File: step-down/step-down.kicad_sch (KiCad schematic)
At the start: 16 parts, among them J1 Conn_01x01_Pin, J2 Conn_01x01_Pin, J4 Conn_01x01_Pin

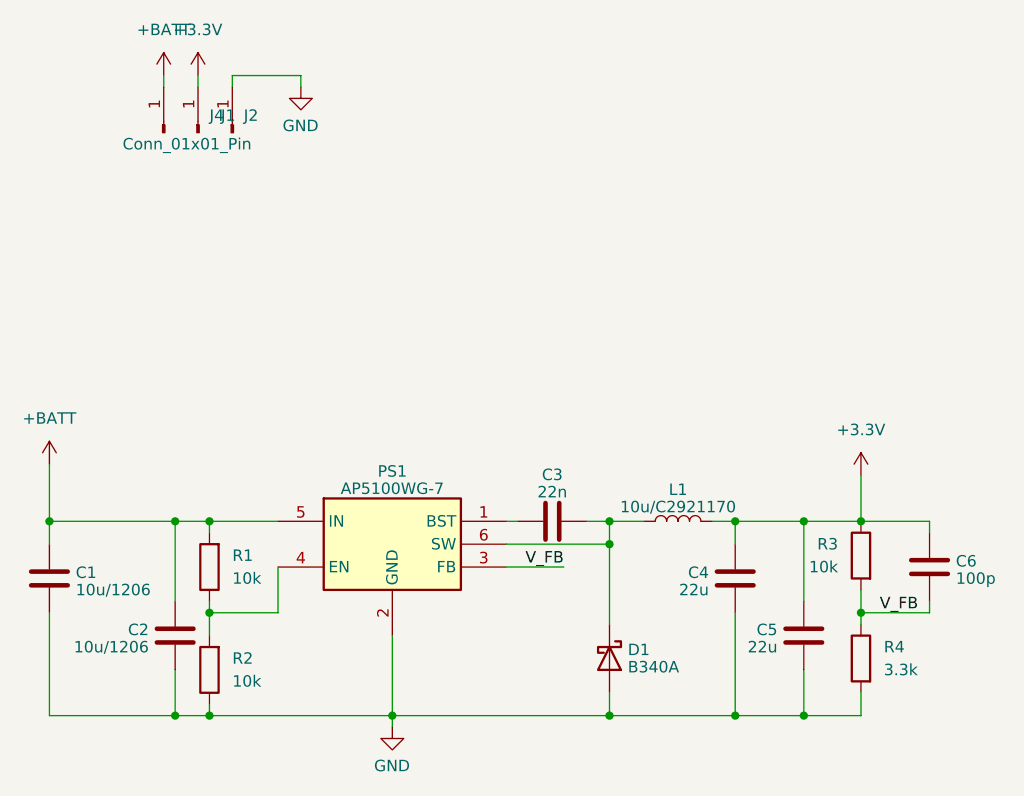
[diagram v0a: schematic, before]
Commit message: moved EN logic to external control
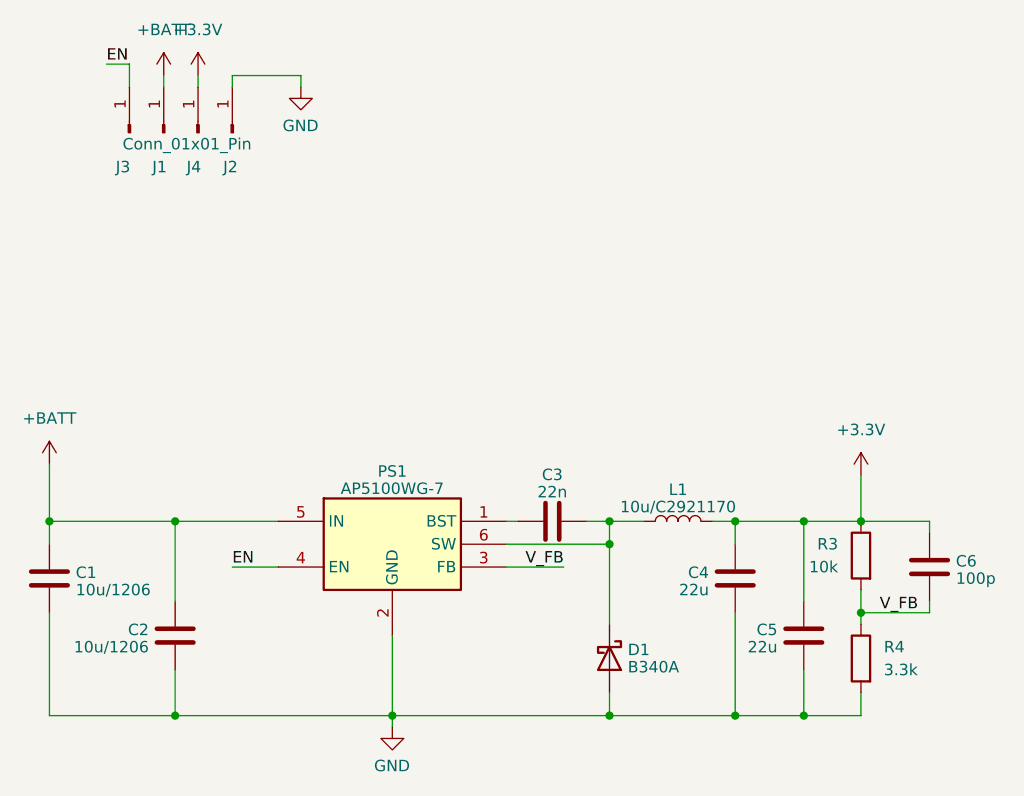
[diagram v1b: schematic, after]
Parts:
- removed R1, R2: 10k, Resistor_SMD:R_0603_1608Metric, symbol Device:R
- added J3: Conn_01x01_Pin, Connector_PinSocket_2.54mm:PinSocket_1x01_P2.54mm_Vertical, symbol Connector:Conn_01x01_Pin
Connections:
- net EN: now reaches PS1.4 (EN)
- net EN: now also J3.1 (Pin_1)
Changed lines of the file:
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@@
 	(paper "A4")
-	(junction
-		(at 109.22 85.09)
-		(diameter 0)
-		(color 0 0 0 0)
-	)
 	(junction
 		(at 91.44 85.09)
@@
 	)
 	(junction
-		(at 109.22 106.68)
-		(diameter 0)
-		(color 0 0 0 0)
-	)
-	(junction
 		(at 105.41 85.09)
 		(diameter 0)
@@
 	)
 	(junction
-		(at 109.22 95.25)
-		(diameter 0)
-		(color 0 0 0 0)
-	)
-	(junction
 		(at 153.67 87.63)
 		(diameter 0)
@@
 	(wire
 		(pts
-			(xy 109.22 97.79) (xy 109.22 95.25)
-		)
-		(stroke
-			(width 0)
-			(type default)
-		)
-	)
-	(wire
-		(pts
 			(xy 189.23 93.98) (xy 189.23 95.25)
 		)
@@
 	(wire
 		(pts
-			(xy 109.22 105.41) (xy 109.22 106.68)
-		)
-		(stroke
-			(width 0)
-			(type default)
-		)
-	)
-	(wire
-		(pts
 			(xy 91.44 78.74) (xy 91.44 85.09)
 		)
@@
 	(wire
 		(pts
-			(xy 109.22 85.09) (xy 109.22 86.36)
-		)
-		(stroke
-			(width 0)
-			(type default)
-		)
-	)
-	(wire
-		(pts
 			(xy 165.1 85.09) (xy 167.64 85.09)
 		)
@@
 	(wire
 		(pts
+			(xy 111.76 90.17) (xy 116.84 90.17)
+		)
+		(stroke
+			(width 0)
+			(type default)
+		)
+	)
+	(wire
+		(pts
 			(xy 91.44 95.25) (xy 91.44 106.68)
 		)
@@
 	(wire
 		(pts
-			(xy 116.84 90.17) (xy 116.84 95.25)
-		)
-		(stroke
-			(width 0)
-			(type default)
-		)
-	)
-	(wire
-		(pts
-			(xy 105.41 106.68) (xy 109.22 106.68)
-		)
-		(stroke
-			(width 0)
-			(type default)
-		)
-	)
-	(wire
-		(pts
 			(xy 181.61 85.09) (xy 189.23 85.09)
 		)
@@
 	(wire
 		(pts
-			(xy 109.22 93.98) (xy 109.22 95.25)
-		)
-		(stroke
-			(width 0)
-			(type default)
-		)
-	)
-	(wire
-		(pts
-			(xy 109.22 106.68) (xy 129.54 106.68)
-		)
-		(stroke
-			(width 0)
-			(type default)
-		)
-	)
-	(wire
-		(pts
-			(xy 109.22 85.09) (xy 116.84 85.09)
+			(xy 105.41 106.68) (xy 129.54 106.68)
+		)
+		(stroke
+			(width 0)
+			(type default)
+		)
+	)
+	(wire
+		(pts
+			(xy 100.33 34.29) (xy 100.33 36.83)
+		)
+		(stroke
+			(width 0)
+			(type default)
+		)
+	)
+	(wire
+		(pts
+			(xy 105.41 85.09) (xy 116.84 85.09)
 		)
 		(stroke
@@
 	(wire
 		(pts
-			(xy 109.22 95.25) (xy 116.84 95.25)
-		)
-		(stroke
-			(width 0)
-			(type default)
-		)
-	)
-	(wire
-		(pts
-			(xy 105.41 85.09) (xy 109.22 85.09)
+			(xy 97.79 34.29) (xy 100.33 34.29)
 		)
 		(stroke
@@
 			)
 			(justify right bottom)
+		)
+	)
+	(label "EN"
+		(at 111.76 90.17 0)
+		(fields_autoplaced yes)
+		(effects
+			(font
+				(size 1.27 1.27)
+			)
+			(justify left bottom)
+		)
+	)
+	(label "EN"
+		(at 97.79 34.29 0)
+		(fields_autoplaced yes)
+		(effects
+			(font
+				(size 1.27 1.27)
+			)
+			(justify left bottom)
 		)
 	)
@@
 		(dnp no)
 		(property "Reference" "J1"
-			(at 110.49 40.0049 90)
+			(at 102.87 45.72 90)
 			(effects
 				(font
@@
 		(dnp no)
 		(property "Reference" "J4"
-			(at 109.22 40.0049 90)
+			(at 106.68 45.72 90)
 			(effects
 				(font
@@
 				(path "/782eae2c-e28e-4a9a-b32f-443cd1a34212"
 					(reference "#PWR03")
-					(unit 1)
-				)
-			)
-		)
-	)
-	(symbol
-		(lib_id "Device:R")
-		(at 109.22 101.6 180)
-		(unit 1)
-		(exclude_from_sim no)
-		(in_bom yes)
-		(on_board yes)
-		(dnp no)
-		(fields_autoplaced yes)
-		(property "Reference" "R2"
-			(at 111.76 100.3299 0)
-			(effects
-				(font
-					(size 1.27 1.27)
-				)
-				(justify right)
-			)
-		)
-		(property "Value" "10k"
-			(at 111.76 102.8699 0)
-			(effects
-				(font
-					(size 1.27 1.27)
-				)
-				(justify right)
-			)
-		)
-		(property "Footprint" "Resistor_SMD:R_0603_1608Metric"
-			(at 110.998 101.6 90)
-			(effects
-				(font
-					(size 1.27 1.27)
-				)
-				(hide yes)
-			)
-		)
-		(property "Datasheet" "~"
-			(at 109.22 101.6 0)
-			(effects
-				(font
-					(size 1.27 1.27)
-				)
-				(hide yes)
-			)
-		)
-		(property "Description" ""
-			(at 109.22 101.6 0)
-			(effects
-				(font
-					(size 1.27 1.27)
-				)
-				(hide yes)
-			)
-		)
-		(property "MPN" "C22975"
-			(at 109.22 101.6 0)
-			(effects
-				(font
-					(size 1.27 1.27)
-				)
-				(hide yes)
-			)
-		)
-		(pin "1"
-		)
-		(pin "2"
-		)
-		(instances
-			(project "step-down"
-				(path "/782eae2c-e28e-4a9a-b32f-443cd1a34212"
-					(reference "R2")
 					(unit 1)
 				)
@@
 		(dnp no)
 		(property "Reference" "J2"
-			(at 113.03 40.0049 90)
+			(at 110.744 45.72 90)
 			(effects
 				(font
@@
 				(path "/782eae2c-e28e-4a9a-b32f-443cd1a34212"
 					(reference "C5")
+					(unit 1)
+				)
+			)
+		)
+	)
+	(symbol
+		(lib_id "Connector:Conn_01x01_Pin")
+		(at 100.33 41.91 90)
+		(unit 1)
+		(exclude_from_sim no)
+		(in_bom yes)
+		(on_board yes)
+		(dnp no)
+		(property "Reference" "J3"
+			(at 98.806 45.72 90)
+			(effects
+				(font
+					(size 1.27 1.27)
+				)
+				(justify right)
+			)
+		)
+		(property "Value" "Conn_01x01_Pin"
+			(at 101.6 42.5449 90)
+			(effects
+				(font
+					(size 1.27 1.27)
+				)
+				(justify right)
+				(hide yes)
+			)
+		)
+		(property "Footprint" "Connector_PinSocket_2.54mm:PinSocket_1x01_P2.54mm_Vertical"
+			(at 100.33 41.91 0)
+			(effects
+				(font
+					(size 1.27 1.27)
+				)
+				(hide yes)
+			)
+		)
+		(property "Datasheet" "~"
+			(at 100.33 41.91 0)
+			(effects
+				(font
+					(size 1.27 1.27)
+				)
+				(hide yes)
+			)
+		)
+		(property "Description" "Generic connector, single row, 01x01, script generated"
+			(at 100.33 41.91 0)
+			(effects
+				(font
+					(size 1.27 1.27)
+				)
+				(hide yes)
+			)
+		)
+		(pin "1"
+		)
+		(instances
+			(project "step-down"
+				(path "/782eae2c-e28e-4a9a-b32f-443cd1a34212"
+					(reference "J3")
 					(unit 1)
 				)
@@
 					(unit 1)
 				)
-			)
-		)
-	)
-	(symbol
-		(lib_id "Device:R")
-		(at 109.22 90.17 180)
-		(unit 1)
-		(exclude_from_sim no)
-		(in_bom yes)
-		(on_board yes)
-		(dnp no)
-		(fields_autoplaced yes)
-		(property "Reference" "R1"
-			(at 111.76 88.8999 0)
-			(effects
-				(font
-					(size 1.27 1.27)
-				)
-				(justify right)
-			)
-		)
-		(property "Value" "10k"
-			(at 111.76 91.4399 0)
-			(effects
-				(font
-					(size 1.27 1.27)
-				)
-				(justify right)
-			)
-		)
-		(property "Footprint" "Resistor_SMD:R_0603_1608Metric"
-			(at 110.998 90.17 90)
-			(effects
-				(font
-					(size 1.27 1.27)
-				)
-				(hide yes)
-			)
-		)
-		(property "Datasheet" "~"
-			(at 109.22 90.17 0)
-			(effects
-				(font
-					(size 1.27 1.27)
-				)
-				(hide yes)
-			)
-		)
-		(property "Description" ""
-			(at 109.22 90.17 0)
-			(effects
-				(font
-					(size 1.27 1.27)
-				)
-				(hide yes)
-			)
-		)
-		(property "MPN" "C25804"
-			(at 109.22 90.17 0)
-			(effects
-				(font
-					(size 1.27 1.27)
-				)
-				(hide yes)
-			)
-		)
-		(pin "1"
-		)
-		(pin "2"
-		)
-		(instances
-			(project "step-down"
-				(path "/782eae2c-e28e-4a9a-b32f-443cd1a34212"
-					(reference "R1")
-					(unit 1)
-				)
